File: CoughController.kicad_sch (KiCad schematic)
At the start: 4 parts, among them J6 電源入力, J7 電源出力

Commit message: カフコントローラ
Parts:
- added H1, H2, H3, H4: MountingHole, MountingHole:MountingHole_3.2mm_M3, symbol Mechanical:MountingHole
- J6: value 電源入力 -> PWR_IN
- J7: value 電源出力 -> PWR_OUT
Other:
- moved on the sheet: J7

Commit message: 端子をピンヘッダ2x10に変更
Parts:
- renumbered J6 to J7, J7 to J8

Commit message: 電源コネクタ　フットプリント間違いを修正
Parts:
- J7, J8: footprint Connector_JST:JST_EH_B2B-EH-A_1x02_P2.50mm_Vertical -> Connector_JST:JST_XH_B2B-XH-AM_1x02_P2.50mm_Vertical
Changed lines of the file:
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@@
       (effects (font (size 1.27 1.27)))
     )
-    (property "Footprint" "Connector_JST:JST_EH_B2B-EH-A_1x02_P2.50mm_Vertical" (at 46.99 74.93 0)
+    (property "Footprint" "Connector_JST:JST_XH_B2B-XH-AM_1x02_P2.50mm_Vertical" (at 46.99 74.93 0)
       (effects (font (size 1.27 1.27)) hide)
     )
@@
       (effects (font (size 1.27 1.27)))
     )
-    (property "Footprint" "Connector_JST:JST_EH_B2B-EH-A_1x02_P2.50mm_Vertical" (at 46.99 50.8 0)
-      (effects (font (size 1.27 1.27)) hide)
-    )
+    (property "Footprint" "Connector_JST:JST_XH_B2B-XH-AM_1x02_P2.50mm_Vertical" (at 46.99 50.8 0)
+      (effects (font (size 1.27 1.27)) hide)
+    )

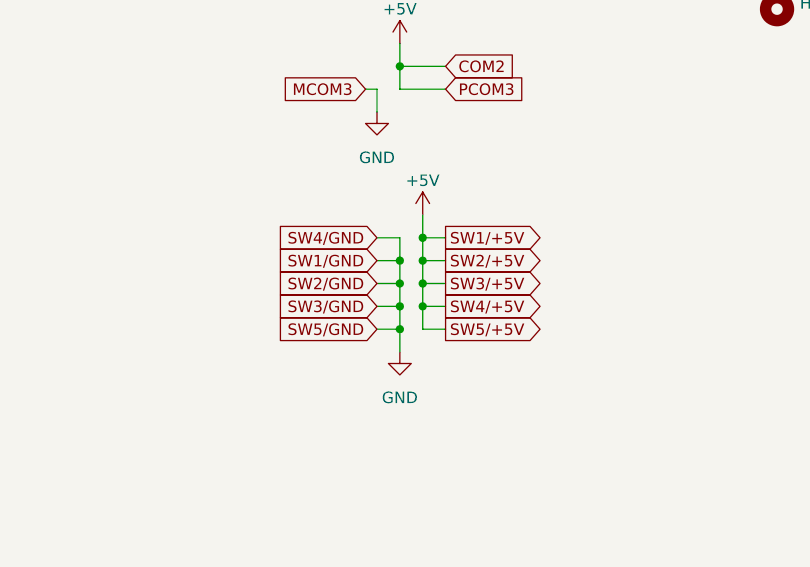
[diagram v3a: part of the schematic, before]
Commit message: SW6/SW7を追加
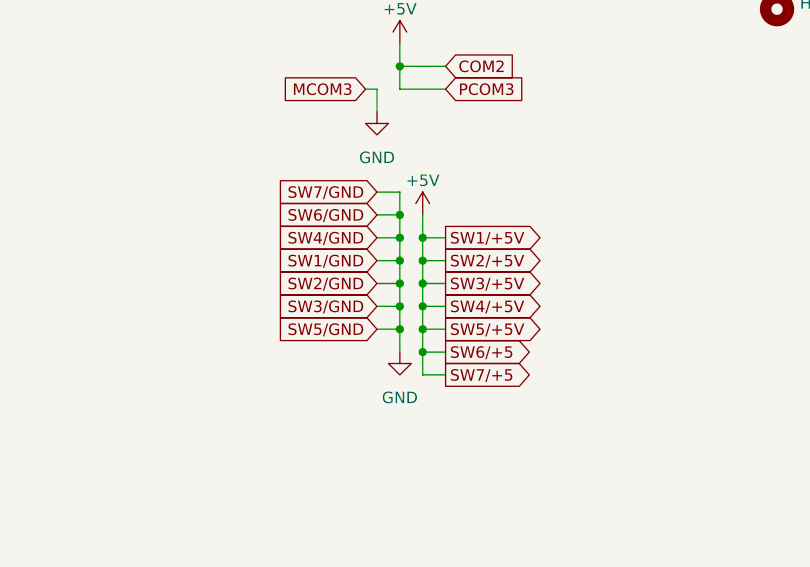
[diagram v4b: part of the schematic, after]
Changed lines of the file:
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@@
   (junction (at 113.03 99.06) (diameter 0) (color 0 0 0 0)
   )
+  (junction (at 113.03 88.9) (diameter 0) (color 0 0 0 0)
+  )
   (junction (at 115.57 96.52) (diameter 0) (color 0 0 0 0)
   )
   (junction (at 113.03 72.39) (diameter 0) (color 0 0 0 0)
   )
+  (junction (at 113.03 91.44) (diameter 0) (color 0 0 0 0)
+  )
   (junction (at 115.57 93.98) (diameter 0) (color 0 0 0 0)
   )
@@
   (junction (at 60.96 48.26) (diameter 0) (color 0 0 0 0)
   )
+  (junction (at 115.57 101.6) (diameter 0) (color 0 0 0 0)
+  )
   (junction (at 113.03 96.52) (diameter 0) (color 0 0 0 0)
   )
@@
   (junction (at 113.03 101.6) (diameter 0) (color 0 0 0 0)
   )
+  (junction (at 115.57 104.14) (diameter 0) (color 0 0 0 0)
+  )
   (wire (pts (xy 115.57 91.44) (xy 115.57 93.98))
     (stroke (width 0) (type default))
   )
+  (wire (pts (xy 113.03 88.9) (xy 113.03 91.44))
+    (stroke (width 0) (type default))
+  )
   (wire (pts (xy 109.22 74.93) (xy 110.49 74.93))
     (stroke (width 0) (type default))
@@
     (stroke (width 0) (type default))
   )
+  (wire (pts (xy 113.03 86.36) (xy 113.03 88.9))
+    (stroke (width 0) (type default))
+  )
+  (wire (pts (xy 118.11 106.68) (xy 115.57 106.68))
+    (stroke (width 0) (type default))
+  )
   (wire (pts (xy 118.11 91.44) (xy 115.57 91.44))
     (stroke (width 0) (type default))
@@
     (stroke (width 0) (type default))
   )
+  (wire (pts (xy 115.57 104.14) (xy 115.57 101.6))
+    (stroke (width 0) (type default))
+  )
   (wire (pts (xy 52.07 50.8) (xy 54.61 50.8))
     (stroke (width 0) (type default))
@@
     (stroke (width 0) (type default))
   )
+  (wire (pts (xy 110.49 88.9) (xy 113.03 88.9))
+    (stroke (width 0) (type default))
+  )
   (wire (pts (xy 118.11 72.39) (xy 113.03 72.39))
     (stroke (width 0) (type default))
@@
     (stroke (width 0) (type default))
   )
+  (wire (pts (xy 115.57 106.68) (xy 115.57 104.14))
+    (stroke (width 0) (type default))
+  )
   (wire (pts (xy 115.57 96.52) (xy 115.57 99.06))
     (stroke (width 0) (type default))
   )
+  (wire (pts (xy 115.57 104.14) (xy 118.11 104.14))
+    (stroke (width 0) (type default))
+  )
   (wire (pts (xy 54.61 48.26) (xy 54.61 45.72))
     (stroke (width 0) (type default))
@@
     (stroke (width 0) (type default))
   )
+  (wire (pts (xy 110.49 86.36) (xy 113.03 86.36))
+    (stroke (width 0) (type default))
+  )
   (wire (pts (xy 52.07 48.26) (xy 54.61 48.26))
     (stroke (width 0) (type default))
@@
     )
   )
+  (global_label "SW6{slash}+5" (shape output) (at 118.11 104.14 0) (fields_autoplaced)
+    (effects (font (size 1.27 1.27)) (justify left))
+    (property "Intersheetrefs" "${INTERSHEET_REFS}" (at 128.9986 104.14 0)
+      (effects (font (size 1.27 1.27)) (justify left) hide)
+    )
+  )
   (global_label "MCOM1" (shape input) (at 109.22 53.34 180) (fields_autoplaced)
     (effects (font (size 1.27 1.27)) (justify right))
@@
     )
   )
+  (global_label "SW6{slash}GND" (shape input) (at 110.49 88.9 180) (fields_autoplaced)
+    (effects (font (size 1.27 1.27)) (justify right))
+    (property "Intersheetrefs" "${INTERSHEET_REFS}" (at 98.5128 88.9 0)
+      (effects (font (size 1.27 1.27)) (justify right) hide)
+    )
+  )
   (global_label "COM0" (shape input) (at 118.11 55.88 0) (fields_autoplaced)
     (effects (font (size 1.27 1.27)) (justify left))
@@
     )
   )
+  (global_label "SW7{slash}GND" (shape input) (at 110.49 86.36 180) (fields_autoplaced)
+    (effects (font (size 1.27 1.27)) (justify right))
+    (property "Intersheetrefs" "${INTERSHEET_REFS}" (at 98.5128 86.36 0)
+      (effects (font (size 1.27 1.27)) (justify right) hide)
+    )
+  )
+  (global_label "SW7{slash}+5" (shape output) (at 118.11 106.68 0) (fields_autoplaced)
+    (effects (font (size 1.27 1.27)) (justify left))
+    (property "Intersheetrefs" "${INTERSHEET_REFS}" (at 128.9986 106.68 0)
+      (effects (font (size 1.27 1.27)) (justify left) hide)
+    )
+  )

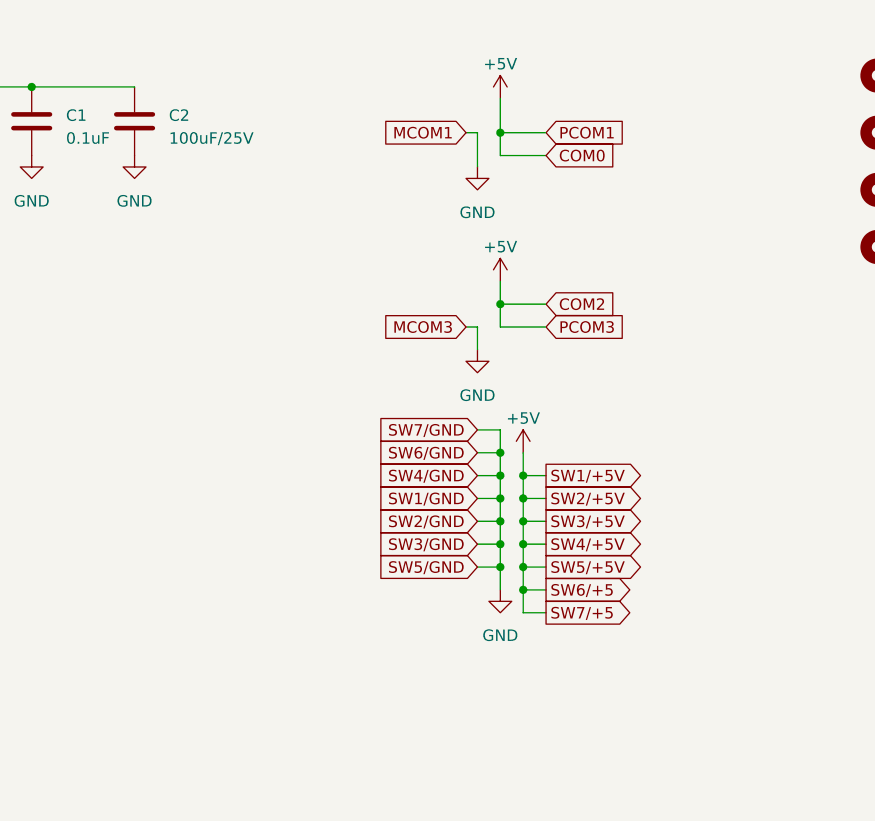
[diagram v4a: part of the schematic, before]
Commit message: bugfix GPIO/IN ドライ接点へ修正
GPIO/INはドライ接点
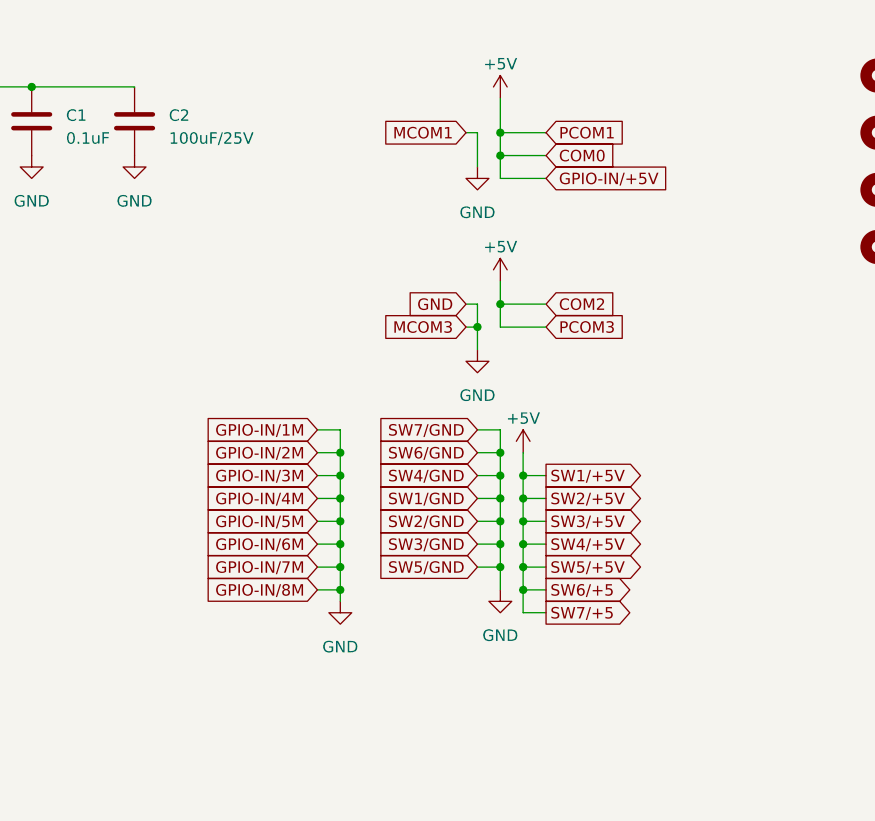
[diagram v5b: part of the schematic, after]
